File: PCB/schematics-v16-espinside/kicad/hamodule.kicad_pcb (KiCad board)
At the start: 2 copper layers, 76.7 x 84.3 mm, 73 parts, among them J1 2604-1104, J10 USB_B_Micro, J2 2604-1102, J4 ESP Relays, J5 Current Jumper, J6 GND 3.3V, J7 Conn_01x02, J8 Current Jumper, J9 2604-1104, K1 PCN-105D, K2 PCN-105D, K3 PCN-105D, K4 PCN-105D, Q1 2N2219, Q2 2N2219, SW1 EN-Switch, SW2 IO0-Switch, U1 ULN2003A, U2 ESP32-WROOM-32D, U3 CP2102N-A01-GQFN24, U4 LD1117AV33_TO220, U6 LDA210-PDIP, U7 LDA210-PDIP

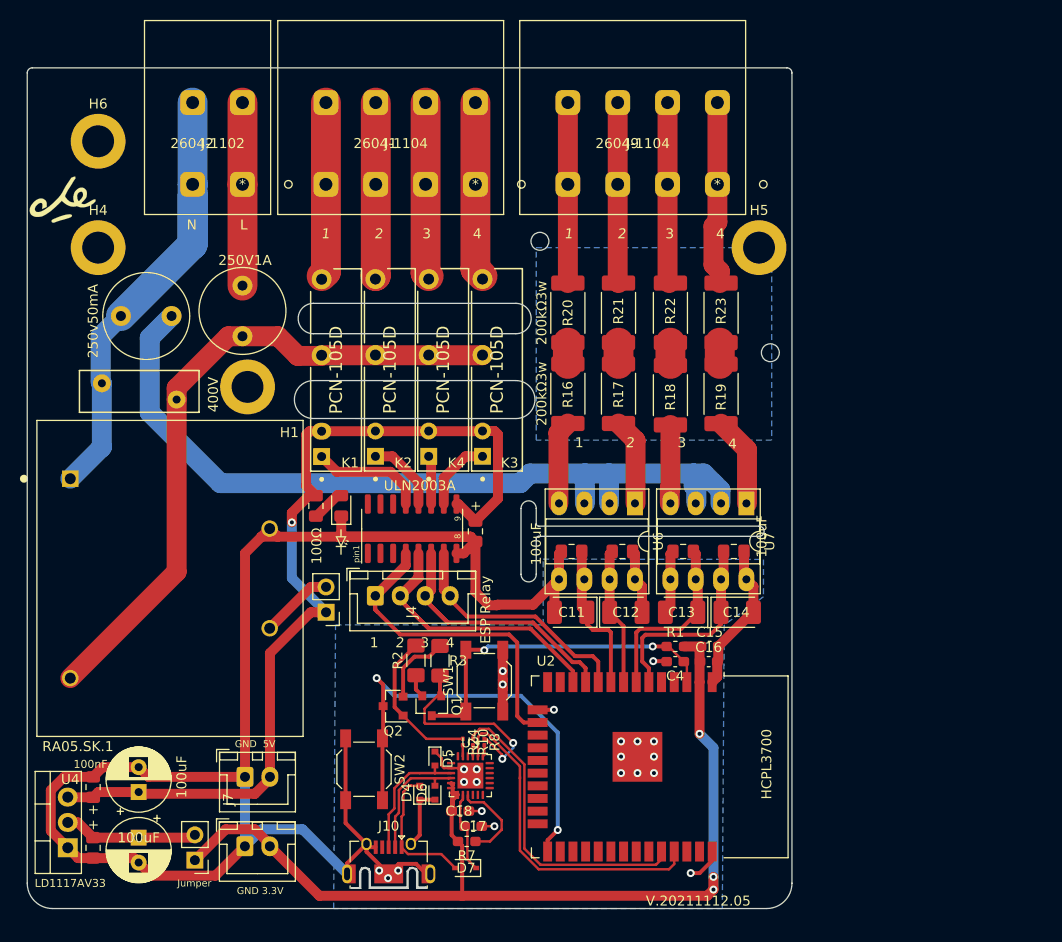
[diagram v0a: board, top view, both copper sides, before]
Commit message: sorting ESP32 components
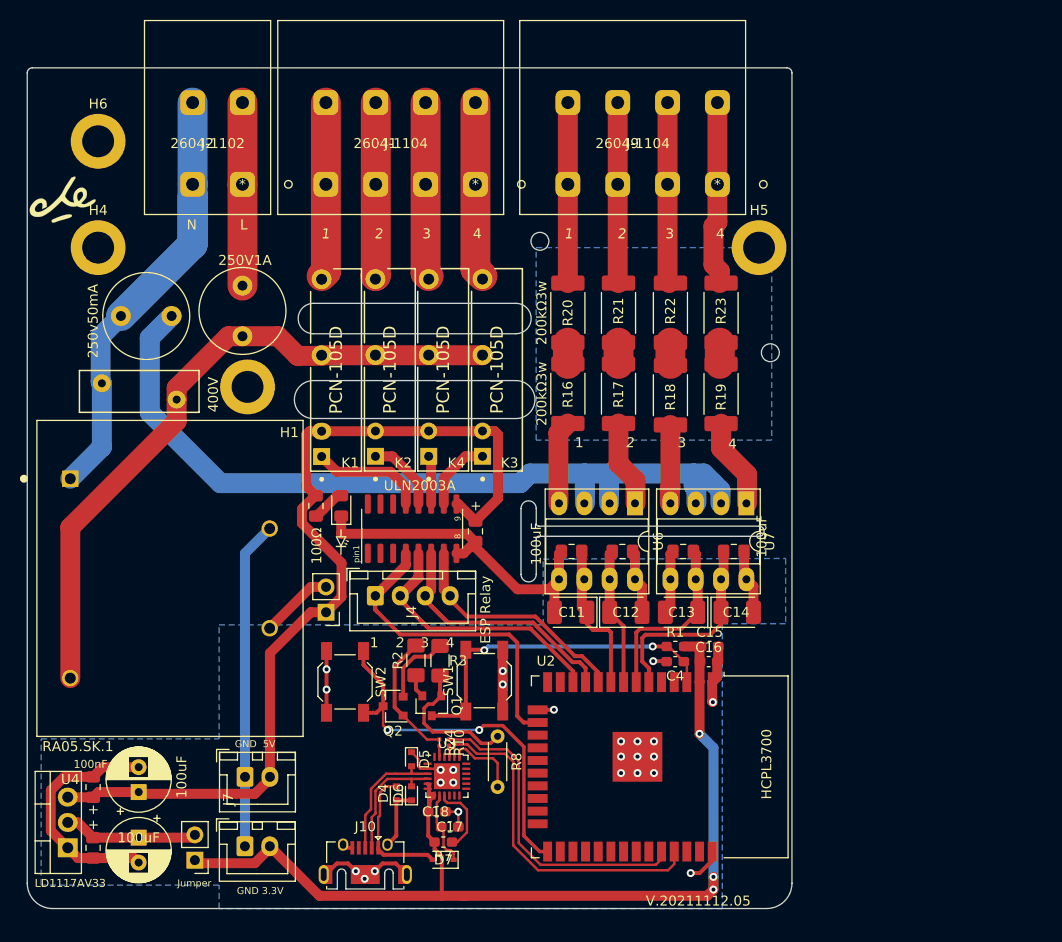
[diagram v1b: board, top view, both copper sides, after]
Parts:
- R8: footprint Resistor_SMD:R_0201_0603Metric -> Resistor_THT:R_Axial_DIN0204_L3.6mm_D1.6mm_P5.08mm_Horizontal
- moved SW2 8.97 mm to (157.0, 129.0)
- moved R10 2.41 mm to (167.4, 135.1)
- moved D7 2.40 mm to (166.9, 146.8)
- moved C17 2.35 mm to (167.5, 143.5)
- moved D4 2.35 mm to (162.2, 140.1)
- moved D5 2.35 mm to (163.7, 136.7)
- moved J10 2.35 mm to (159.1, 148.3)
- moved R7 2.35 mm to (166.9, 145.0)
- moved U3 2.35 mm to (167.3, 138.4)
- moved C18 2.35 mm to (166.2, 142.0)
- moved D6 2.35 mm to (163.7, 140.1)
- moved R24 2.35 mm to (166.5, 135.1)
- moved R8 1.45 mm to (172.3, 134.4)
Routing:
- net GND(5V): track 235.7 -> 160.2 mm, vias 22 -> 25
- net IO0: track 45.3 -> 37.9 mm
- net Net-(R8-Pad2): track 1.17 -> 7.53 mm
- net RTS: track 20.3 -> 14.3 mm, vias 2 -> 0
- net DTR: track 15.2 -> 12.9 mm
- net Net-(R7-Pad1): track 8.78 -> 7.29 mm
- net RXD0: track 31.1 -> 32.4 mm
- net 3.3V+: track 99.6 -> 98.5 mm
- net TXD0: track 34.0 -> 34.9 mm
- net VDD5V: track 8.10 -> 7.47 mm
- net EspRel1: track 24.4 -> 23.8 mm
- net 5V+: track 93.8 -> 93.9 mm, vias 1 -> 0
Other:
- outline, holes or cut-outs redrawn

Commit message: using the right USB connector. We need Mode B
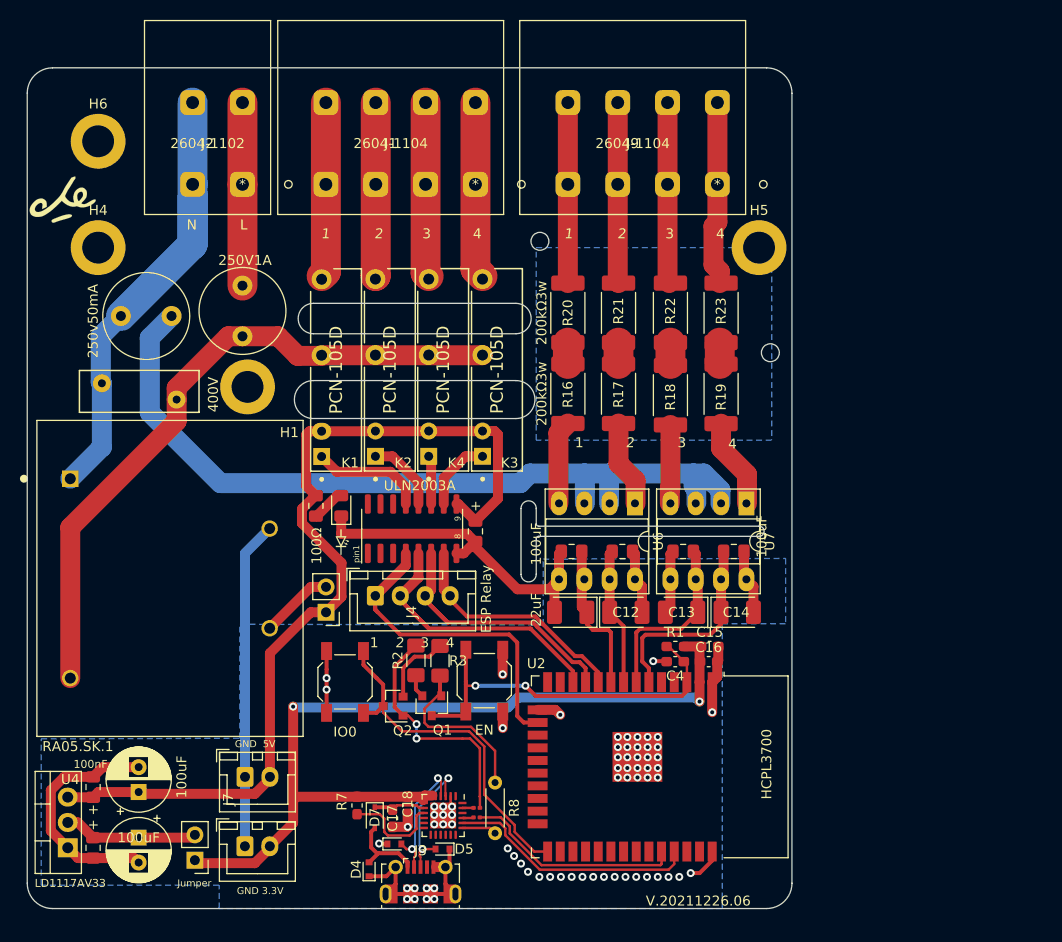
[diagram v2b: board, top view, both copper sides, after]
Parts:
- removed J10: USB_B_Micro, Connector_USB:USB_Micro-AB_Molex_47590-0001
- added J3: USB_B_Micro, Connector_USB:USB_Micro-B_Molex-105017-0001, F.Cu at (164.6, 149.0)
- SW1: value EN-Switch -> EN
- SW2: value IO0-Switch -> IO0
- moved D5 9.54 mm to (166.8, 145.7), turned to 180 degrees
- moved R7 9.40 mm to (158.2, 141.4), turned to 90 degrees
- moved D4 8.10 mm to (159.4, 147.8)
- moved D7 8.05 mm to (160.0, 142.6), turned to 270 degrees
- moved R10 8.00 mm to (170.2, 142.6), turned to 180 degrees
- moved R24 7.54 mm to (170.2, 141.6), turned to 180 degrees
- moved C17 5.81 mm to (161.8, 142.6), turned to 270 degrees
- moved D6 5.36 mm to (162.0, 145.2), turned to 0 degrees
- moved R8 4.64 mm to (172.1, 139.1)
- moved U3 3.96 mm to (166.9, 142.4), turned to 270 degrees
- moved C18 2.99 mm to (163.3, 141.4), turned to 270 degrees
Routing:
- net 3.3V+: track 98.5 -> 86.6 mm, vias 3 -> 2
- net DTR: track 12.9 -> 24.1 mm, vias 0 -> 2
- net RXD0: track 32.4 -> 21.9 mm
- net TXD0: track 34.9 -> 25.1 mm
- net Net-(D4-Pad2): track 13.6 -> 8.27 mm
- net GND(5V): track 160.2 -> 165.2 mm, vias 25 -> 70
- net Net-(R8-Pad2): track 7.53 -> 3.49 mm
- net EN: track 34.6 -> 38.1 mm
- net IO0: track 37.9 -> 34.8 mm, vias 2 -> 0
- net RTS: track 14.3 -> 17.1 mm
- net Net-(R7-Pad1): track 7.29 -> 10.1 mm
- net VDD5V: track 7.47 -> 5.31 mm
- net D-: track 12.4 -> 13.4 mm, vias 0 -> 2
- net D+: track 13.3 -> 13.7 mm, vias 0 -> 2
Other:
- outline, holes or cut-outs redrawn
- board text added: "V.20211226.06"
- board text removed: "V.20211112.05"

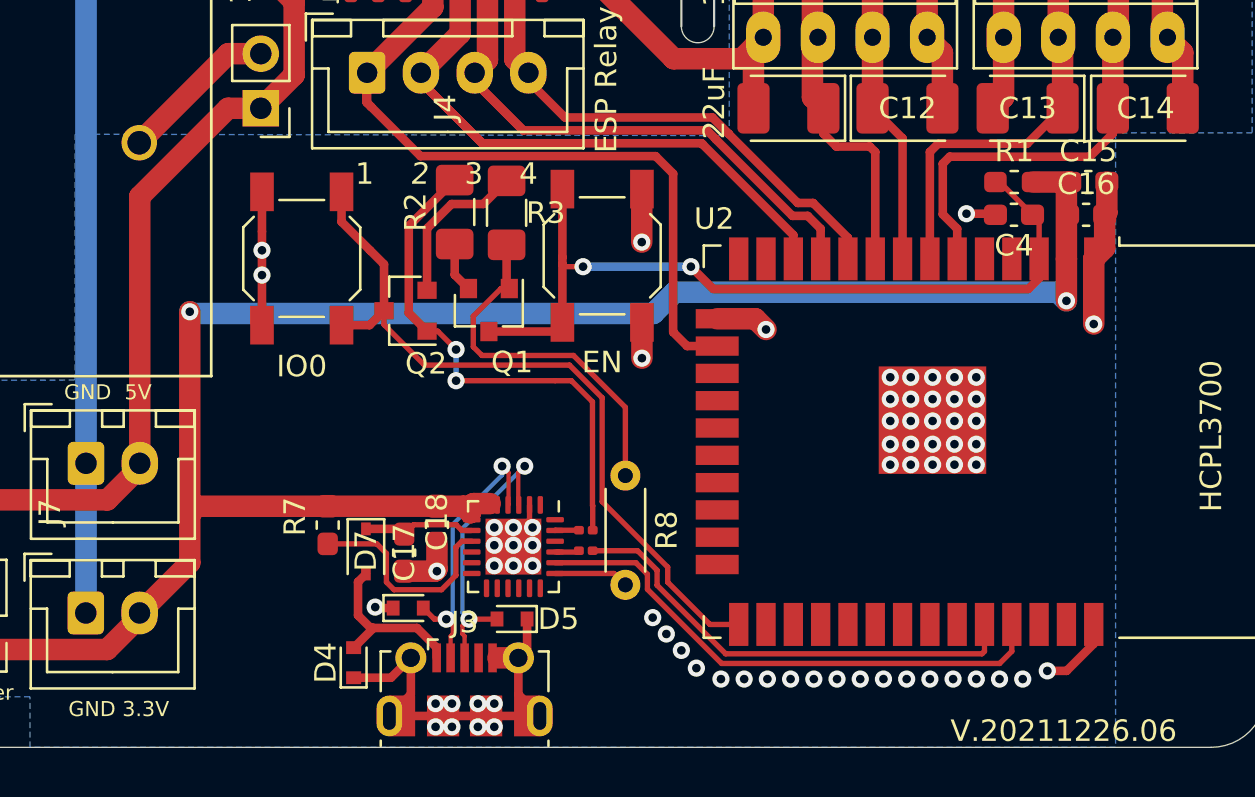
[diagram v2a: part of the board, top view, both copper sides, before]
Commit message: copying USB part from DevKit, adding missing caps, 0Ohm resistors for TXRX
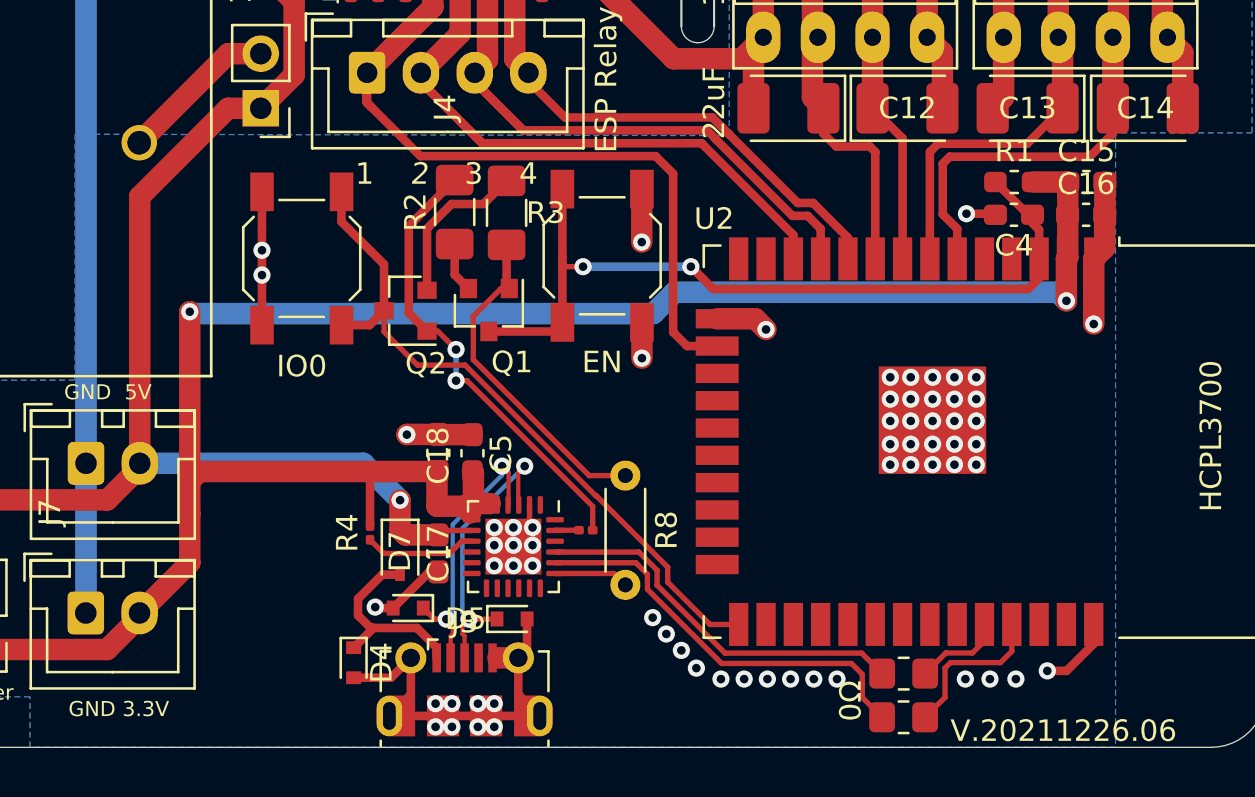
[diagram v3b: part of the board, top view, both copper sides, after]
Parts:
- removed R10: 1kΩ, Resistor_SMD:R_0201_0603Metric
- removed R7: 10kΩ, Resistor_SMD:R_0603_1608Metric_Pad1.05x0.95mm_HandSolder
- added C5: 4.7uF, Capacitor_SMD:C_0603_1608Metric_Pad1.08x0.95mm_HandSolder, F.Cu at (165.0, 138.0)
- added R4: 1kΩ, Resistor_SMD:R_0201_0603Metric, F.Cu at (160.2, 141.7)
- added R5: 0Ω, Resistor_SMD:R_0805_2012Metric_Pad1.20x1.40mm_HandSolder, F.Cu at (185.0, 150.3)
- added R6: 0Ω, Resistor_SMD:R_0805_2012Metric_Pad1.20x1.40mm_HandSolder, F.Cu at (185.0, 148.3)
- D7: value BAT60A -> BAT60A-7
- moved C18 3.34 mm to (163.4, 138.0), turned to 90 degrees
- moved C17 1.59 mm to (163.4, 142.7)
- moved D7 1.59 mm to (161.6, 142.6)
- moved C15 0.09 mm to (193.5, 125.4)
- turned D4 to 270 degrees
- turned D5 to 0 degrees
- turned D6 to 180 degrees
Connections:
- C17 pad 1: VDD5V -> 5V+
- D4 pad 1: GND(5V) -> Net-(D4-Pad1)
- D4 pad 2: Net-(D4-Pad2) -> GND(5V)
- D5 pad 1: GND(5V) -> D+
- D5 pad 2: D+ -> GND(5V)
- D6 pad 1: GND(5V) -> D-
- D6 pad 2: D- -> GND(5V)
- D7 pad 1: VDD5V -> 5V+
- D7 pad 2: Net-(D4-Pad2) -> Net-(D4-Pad1)
- J3 pad 1: Net-(D4-Pad2) -> Net-(D4-Pad1)
- U3 pad 20: TXD0 -> Net-(R5-Pad2)
- U3 pad 8: VDD5V -> 5V+
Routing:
- net Net-(R5-Pad2): track 0.00 -> 19.2 mm
- net RXD0: track 21.9 -> 4.15 mm
- net TXD0: track 25.1 -> 7.35 mm
- net 5V+: track 93.9 -> 111.6 mm, vias 0 -> 1
- net Net-(R6-Pad2): track 1.11 -> 18.0 mm
- net Net-(D4-Pad1): track 0.00 -> 9.39 mm
- net Net-(D4-Pad2): track 8.27 -> 0.00 mm
- net 3.3V+: track 86.6 -> 92.4 mm
- net VDD5V: track 5.31 -> 0.00 mm
- net Net-(R4-Pad1): track 10.1 -> 5.23 mm
- net DTR: track 24.1 -> 21.3 mm
- net IO0: track 34.8 -> 32.1 mm
- net RTS: track 17.1 -> 15.6 mm
- net GND(5V): track 165.2 -> 165.5 mm, vias 70 -> 65

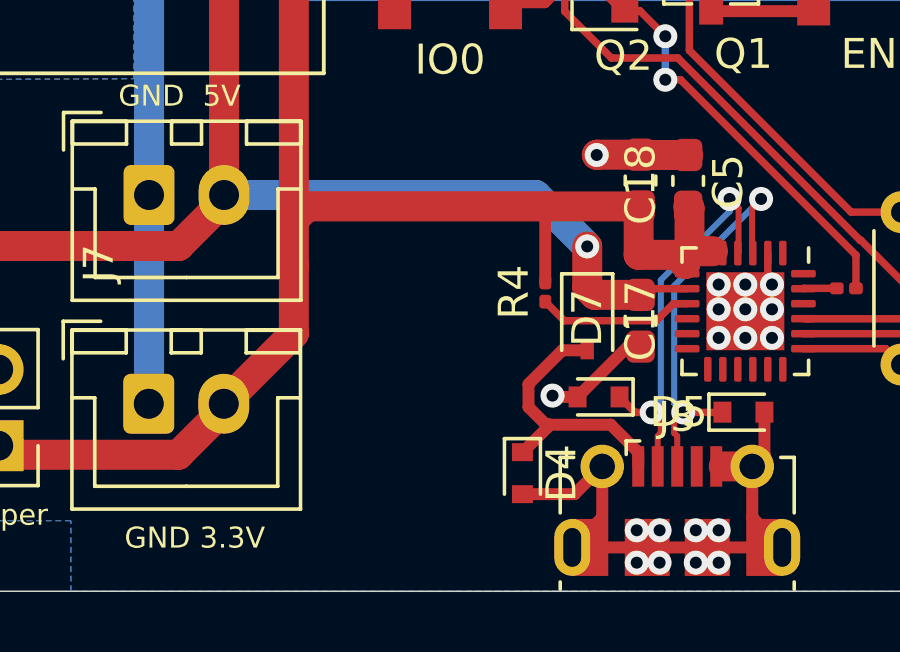
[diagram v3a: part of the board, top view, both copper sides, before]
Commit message: VBus is signaling the CP2102 before the diode (+resistors), and driving the 5V->3V after the diode
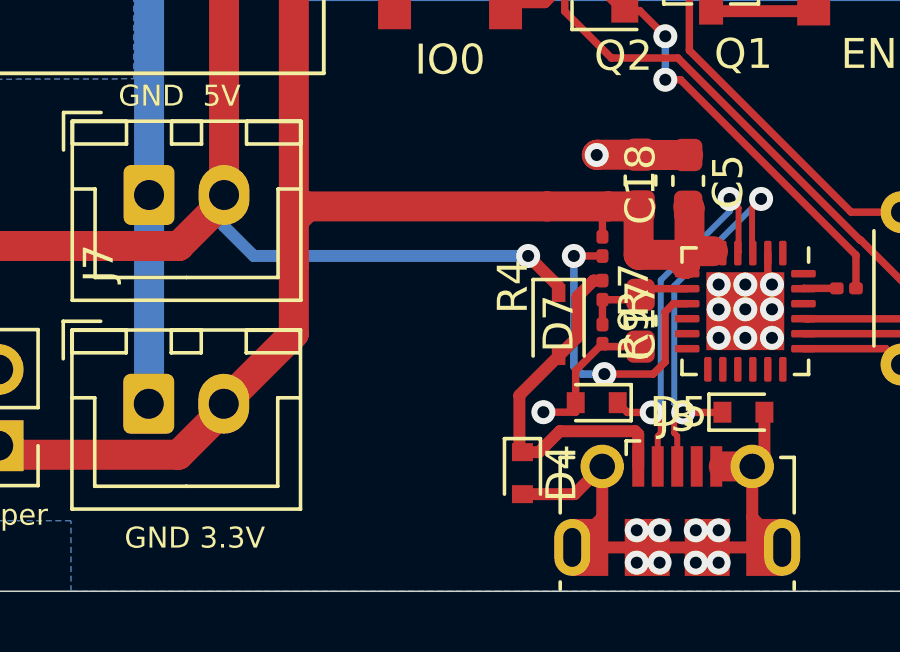
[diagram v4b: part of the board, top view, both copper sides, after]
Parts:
- added R7: 22.1kΩ, Resistor_SMD:R_0201_0603Metric, F.Cu at (162.1, 141.7)
- added R9: 47.5kΩ, Resistor_SMD:R_0201_0603Metric, F.Cu at (162.1, 143.1)
- moved R4 2.44 mm to (162.1, 140.2)
- moved D7 0.97 mm to (160.7, 142.8)
- moved D6 0.20 mm to (161.9, 145.4)
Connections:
- net Net-(D4-Pad1) renamed VBUS
- C17 pad 1: 5V+ -> Net-(C17-Pad1)
- U3 pad 8: 5V+ -> Net-(C17-Pad1)
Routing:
- net Net-(R4-Pad1): track 5.23 -> 10.5 mm, vias 0 -> 2
- net 5V+: track 111.6 -> 107.1 mm
- net Net-(C17-Pad1): track 0.00 -> 3.80 mm
- net VBUS: track 9.39 -> 12.3 mm
- net 3.3V+: track 92.4 -> 90.9 mm
- net GND(5V): track 165.5 -> 166.9 mm
